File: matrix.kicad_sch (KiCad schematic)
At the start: 152 parts, among them SW1 MX_SW_solder, SW10 MX_SW_solder, SW11 MX_SW_solder, SW12 MX_SW_solder, SW13 MX_SW_solder, SW14 MX_SW_solder, SW15 MX_SW_solder, SW16 MX_SW_solder, SW17 MX_SW_solder, SW18 MX_SW_solder, SW19 MX_SW_solder, SW2 MX_SW_solder, SW20 MX_SW_solder, SW21 MX_SW_solder, SW22 MX_SW_solder, SW23 MX_SW_solder, SW24 MX_SW_solder, SW25 MX_SW_solder, SW26 MX_SW_solder, SW27 MX_SW_solder, SW28 MX_SW_solder, SW29 MX_SW_solder, SW3 MX_SW_solder, SW30 MX_SW_solder, SW31 MX_SW_solder, SW32 MX_SW_solder, SW33 MX_SW_solder, SW34 MX_SW_solder, SW35 MX_SW_solder, SW36 MX_SW_solder, SW37 MX_SW_solder, SW38 MX_SW_solder, SW39 MX_SW_solder, SW4 MX_SW_solder, SW40 MX_SW_solder, SW41 MX_SW_solder, SW42 MX_SW_solder, SW43 MX_SW_solder, SW44 MX_SW_solder, SW45 MX_SW_solder, SW46 MX_SW_solder, SW47 MX_SW_solder, SW48 MX_SW_solder, SW49 MX_SW_solder, SW5 MX_SW_solder, SW50 MX_SW_solder, SW51 MX_SW_solder, SW52 MX_SW_solder, SW53 MX_SW_solder, SW54 MX_SW_solder, SW55 MX_SW_solder, SW56 MX_SW_solder, SW57 MX_SW_solder, SW58 MX_SW_solder, SW59 MX_SW_solder, SW6 MX_SW_solder, SW60 MX_SW_solder, SW61 MX_SW_solder, SW62 MX_SW_solder, SW63 MX_SW_solder, SW64 MX_SW_solder, SW65 MX_SW_solder, SW66 MX_SW_solder, SW67 MX_SW_solder, SW68 MX_SW_solder, SW69 MX_SW_solder, SW7 MX_SW_solder, SW70 MX_SW_solder, SW71 MX_SW_solder, SW72 MX_SW_solder, SW73 MX_SW_solder, SW74 MX_SW_solder, SW75 MX_SW_solder, SW76 MX_SW_solder, SW77 MX_SW_solder, SW78 MX_SW_solder, SW79 MX_SW_solder, SW8 MX_SW_solder, SW80 MX_SW_solder, SW81 MX_SW_solder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

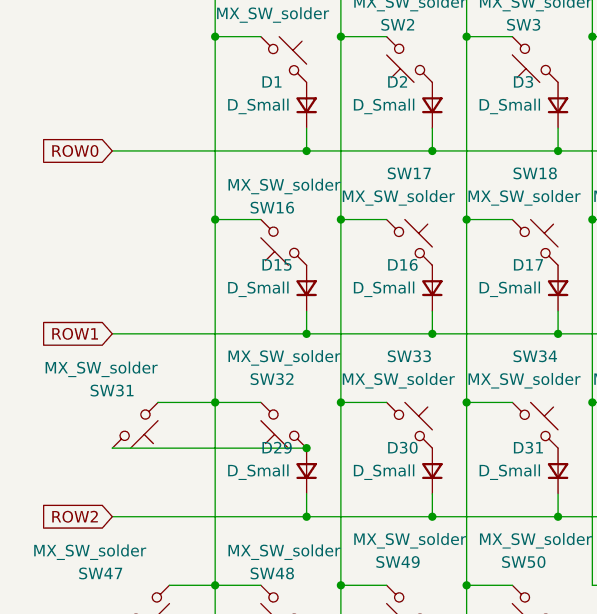
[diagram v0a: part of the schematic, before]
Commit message: add capslock in-switch LED indicator
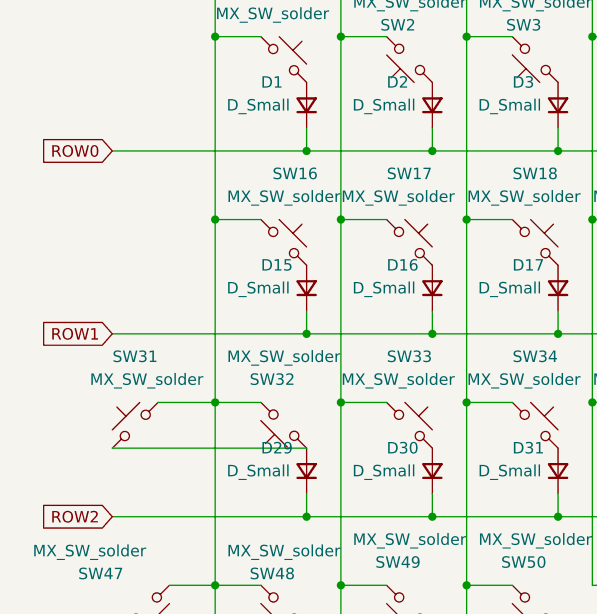
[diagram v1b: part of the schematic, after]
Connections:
- net COL00: now also SW16.1, SW31.1; no longer SW16.2, SW31.2
- net at D15.2 (A): now also SW16.2; no longer SW16.1
- net at D29.2 (A), SW32.1: now also SW31.2; no longer SW31.1
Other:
- moved on the sheet: SW16
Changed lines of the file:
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@@
   (junction (at 185.42 48.26) (diameter 0) (color 0 0 0 0)
-  )
-  (junction (at 45.72 81.28) (diameter 0) (color 0 0 0 0)
   )
   (junction (at 233.68 76.2) (diameter 0) (color 0 0 0 0)
@@
     (pin "2")
   )
-  (symbol (lib_id "marbastlib-mx:MX_SW_solder") (at 43.18 58.42 180) (unit 1)
-    (in_bom yes) (on_board yes)
-    (property "Reference" "SW16" (id 0) (at 41.91 54.61 0))
-    (property "Value" "MX_SW_solder" (id 1) (at 43.18 52.07 0))
+  (symbol (lib_id "marbastlib-mx:MX_SW_solder") (at 43.18 58.42 0) (unit 1)
+    (in_bom yes) (on_board yes)
+    (property "Reference" "SW16" (id 0) (at 44.45 50.8 0))
+    (property "Value" "MX_SW_solder" (id 1) (at 43.18 53.34 0))
     (property "Footprint" "marbastlib-mx:SW_MX_1.5u" (id 2) (at 43.18 58.42 0)
       (effects (font (size 1.27 1.27)) hide)
@@
     (pin "2")
   )
-  (symbol (lib_id "marbastlib-mx:MX_SW_solder") (at 26.67 78.74 0) (mirror x) (unit 1)
-    (in_bom yes) (on_board yes)
-    (property "Reference" "SW31" (id 0) (at 24.13 74.93 0))
-    (property "Value" "MX_SW_solder" (id 1) (at 22.86 72.39 0))
+  (symbol (lib_id "marbastlib-mx:MX_SW_solder") (at 26.67 78.74 0) (mirror y) (unit 1)
+    (in_bom yes) (on_board yes)
+    (property "Reference" "SW31" (id 0) (at 26.67 71.12 0))
+    (property "Value" "MX_SW_solder" (id 1) (at 27.94 73.66 0))
     (property "Footprint" "marbastlib-mx:SW_MX_1.75u_stp" (id 2) (at 26.67 78.74 0)
       (effects (font (size 1.27 1.27)) hide)

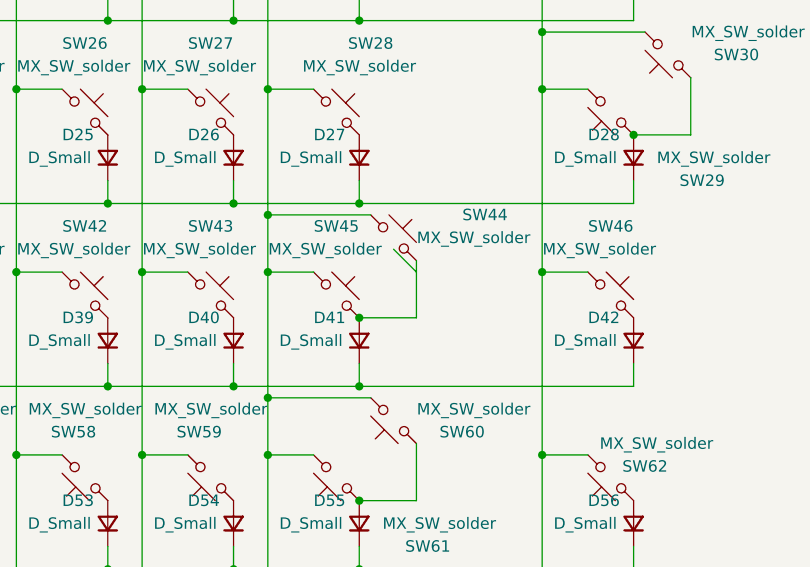
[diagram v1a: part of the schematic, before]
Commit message: add part numbers for BOM
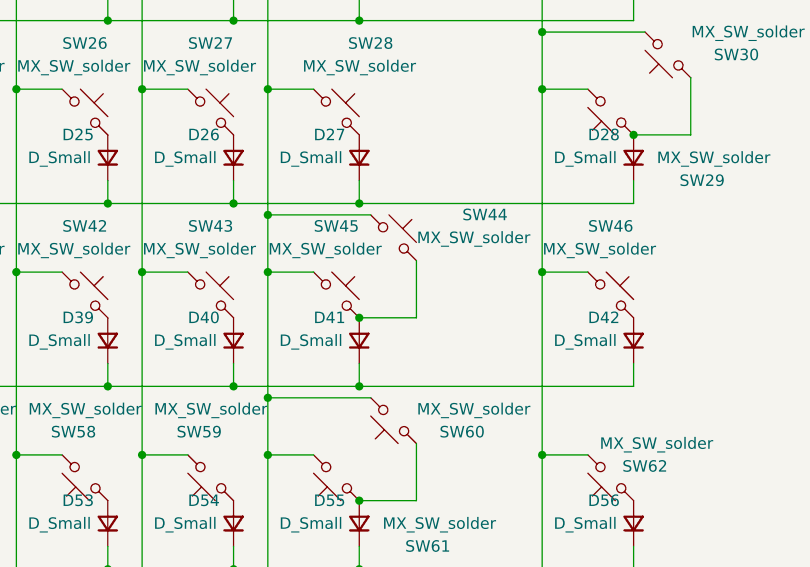
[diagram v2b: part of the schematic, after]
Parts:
- D1, D10, D11, D12, D13, D14, D15, D16, D17, D18, D19, D2, D20, D21, D22, D23, D24, D25, D26, D27, D28, D29, D3, D30, D31, D32, D33, D34, D35, D36, D37, D38, D39, D4, D40, D41, D42, D43, D44, D45, D46, D47, D48, D49, D5, D50, D51, D52, D53, D54, D55, D56, D57, D58, D59, D6, D60, D61, D62, D63, D64, D65, D66, D7, D8, D9: LCSC (none) -> C81598
- SW1, SW10, SW11, SW12, SW13, SW14, SW15, SW16, SW17, SW18, SW19, SW2, SW20, SW21, SW22, SW23, SW24, SW25, SW26, SW27, SW28, SW29, SW3, SW30, SW31, SW32, SW33, SW34, SW35, SW36, SW37, SW38, SW39, SW4, SW40, SW41, SW42, SW43, SW44, SW45, SW46, SW47, SW48, SW49, SW5, SW50, SW51, SW52, SW53, SW54, SW55, SW56, SW57, SW58, SW59, SW6, SW60, SW61, SW62, SW63, SW64, SW65, SW66, SW67, SW68, SW69, SW7, SW70, SW71, SW72, SW73, SW74, SW75, SW76, SW77, SW78, SW79, SW8, SW80, SW81, SW82, SW83, SW84, SW85, SW86, SW9: now left out of the parts list
